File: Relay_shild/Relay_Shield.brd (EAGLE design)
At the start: 56.4 x 30 mm, 11 parts, among them K1 G2RE, T1 2N2222

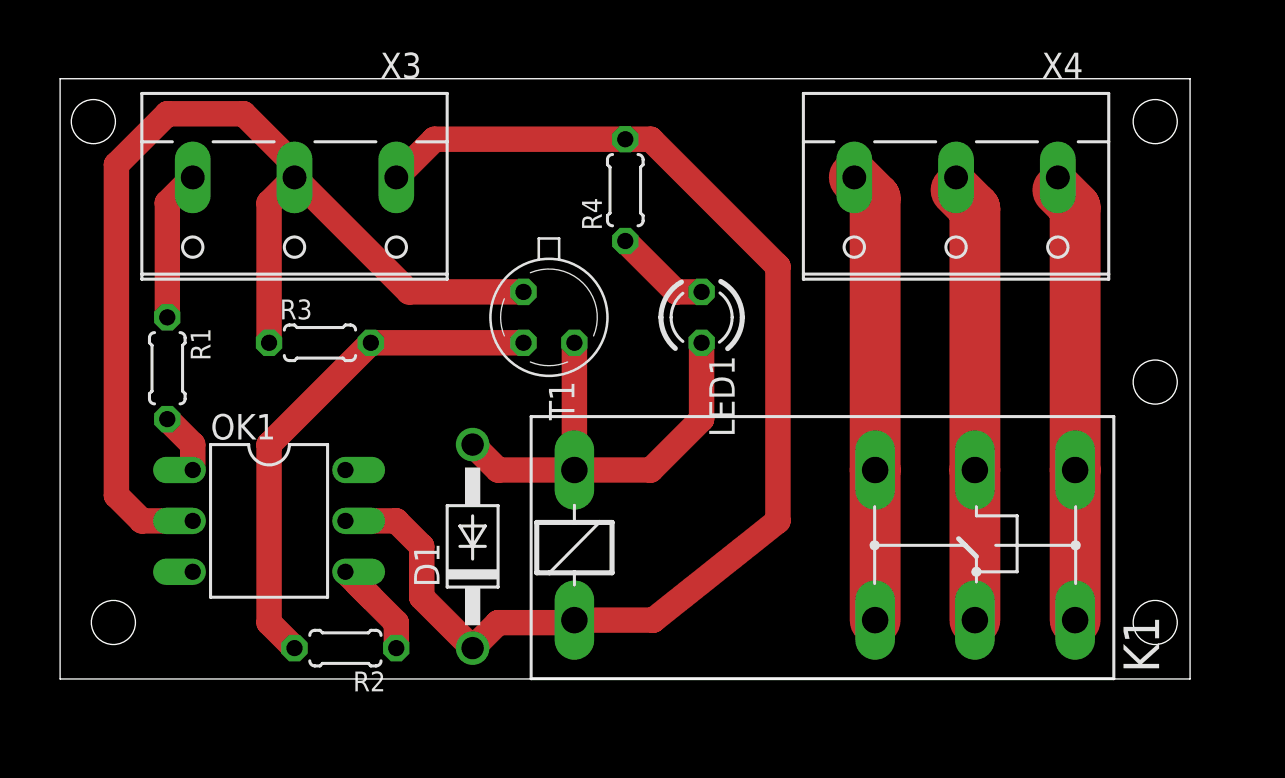
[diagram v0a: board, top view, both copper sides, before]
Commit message: added port extender, modified relay shield
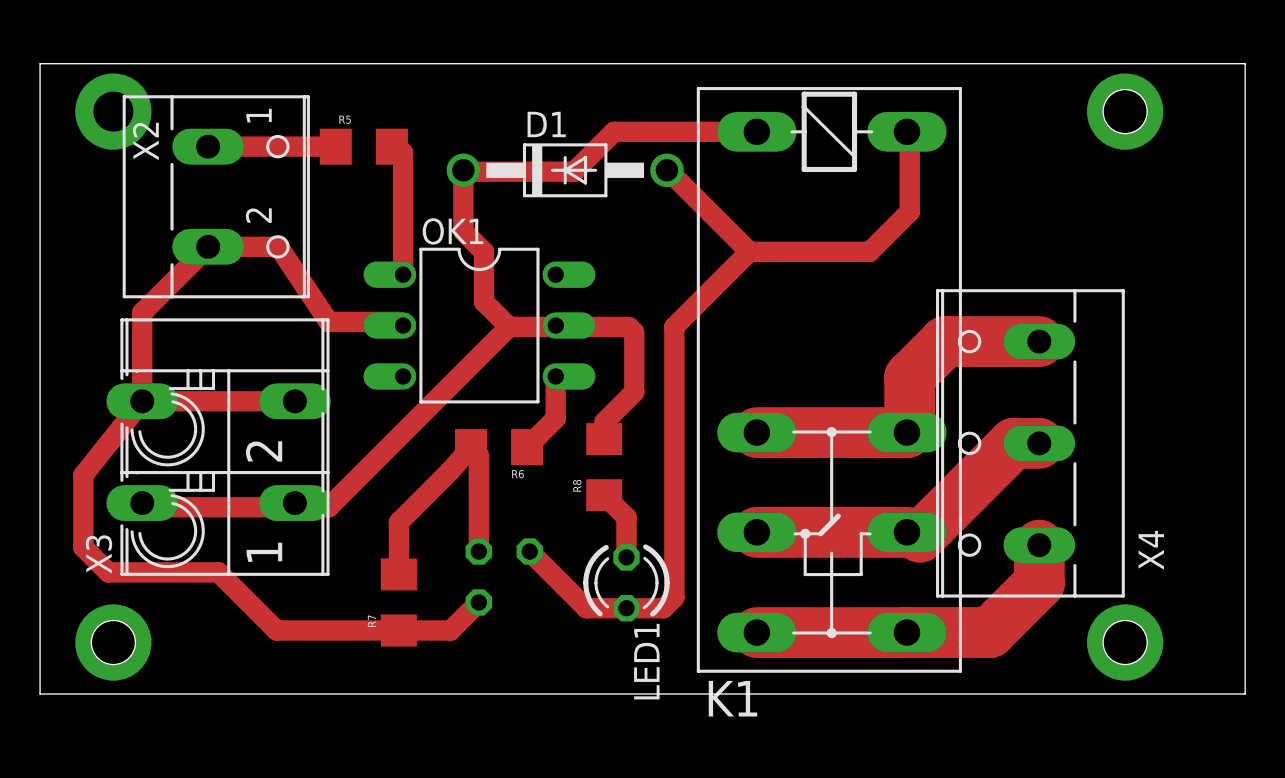
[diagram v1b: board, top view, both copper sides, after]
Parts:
- removed R1, R2: 1K, rcl:0204/5
- removed R3: 10K, rcl:0204/5
- removed R4: 1.1K, rcl:0204/5
- added R5, R6: 1K, SparkFun-Passives:1206
- added R7: 10k, SparkFun-Passives:1206
- added R8: 1.1K, SparkFun-Passives:1206
- added X2: (no value), con-wago-500:W237-102
- X3: value (none) -> FFKV2; device con-wago-508:W237-3E -> con-phoenix-508:FFKV2
- moved K1 20.8 mm to (92.8, 69.0), turned to 270 degrees
- moved D1 19.3 mm to (79.5, 69.6), turned to 0 degrees
- moved OK1 14.3 mm to (75.3, 61.8)
- moved LED1 13.8 mm to (82.6, 49.0)
- moved X3 13.6 mm to (62.2, 55.5), turned to 90 degrees
- moved T1 13.2 mm to (76.5, 49.3), flipped to the bottom, turned to 90 degrees
- moved X4 13.1 mm to (102.6, 55.9), turned to 90 degrees
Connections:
- net +24V: now also R8.2, X3.1A; no longer R4.2, X3.1
- net GND: now also R7.1, X2.2, X3.2A; no longer R3.1, X3.2
- net N$1: now also R5.2; no longer R1.2
- net N$2: now also R6.1; no longer R2.1
- net N$3: now also R6.2, R7.2; no longer R2.2, R3.2
- net N$4: now also R5.1, X2.1; no longer R1.1, X3.3
- net N$6: now also R8.1; no longer R4.1
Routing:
- net N$5: track 23.2 -> 46.1 mm
- net N$3: track 25.5 -> 13.3 mm
- net N$8: track 21.9 -> 15.4 mm
- net N$9: track 22.5 -> 17.5 mm
- net N$10: track 21.8 -> 17.0 mm
- net +24V: track 63.2 -> 58.8 mm
- net N$1: track 3.07 -> 6.72 mm
- net GND: track 55.7 -> 59.1 mm
- net N$2: track 5.76 -> 4.12 mm
- net N$6: track 4.86 -> 3.56 mm
- net N$4: track 7.51 -> 6.37 mm
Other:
- board size 56.4 x 30 mm -> 60.1 x 31.5 mm
